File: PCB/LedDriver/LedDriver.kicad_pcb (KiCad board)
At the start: 2 copper layers, 125.7 x 125.7 mm, 189 parts, among them J101 LCD, J102 Conn_01x07_Female, J103 Conn_01x02_Male, J104 Conn_01x02_Male, J105 Conn_01x02_Male, J106 Conn_01x02_Male, J107 DC+5V, J108 Conn_01x08_Male, J109 Conn_01x08_Male, J110 Conn_01x08_Male, J111 Conn_01x02_Male, SW101 SW_Push, SW102 SW_Push, SW103 SW_Push, SW104 SW_Push, SW105 SW_Push, SW106 SW_Push, SW107 SW_Push, U101 MW-R-WX, U102 LM1117-3.3, U103 LM35-LP, U201 NJW4617DL3-TE1, U202 NJW4617DL3-TE1, U203 NJW4617DL3-TE1, U204 NJW4617DL3-TE1, U205 NJW4617DL3-TE1, U206 NJW4617DL3-TE1, U207 NJW4617DL3-TE1, U208 74HC595, U301 NJW4617DL3-TE1, U302 NJW4617DL3-TE1, U303 NJW4617DL3-TE1, U304 NJW4617DL3-TE1, U305 NJW4617DL3-TE1, U306 NJW4617DL3-TE1, U307 NJW4617DL3-TE1, U308 74HC595, U401 NJW4617DL3-TE1, U402 NJW4617DL3-TE1, U403 NJW4617DL3-TE1, U404 NJW4617DL3-TE1, U405 NJW4617DL3-TE1, U406 NJW4617DL3-TE1, U407 NJW4617DL3-TE1, U408 74HC595

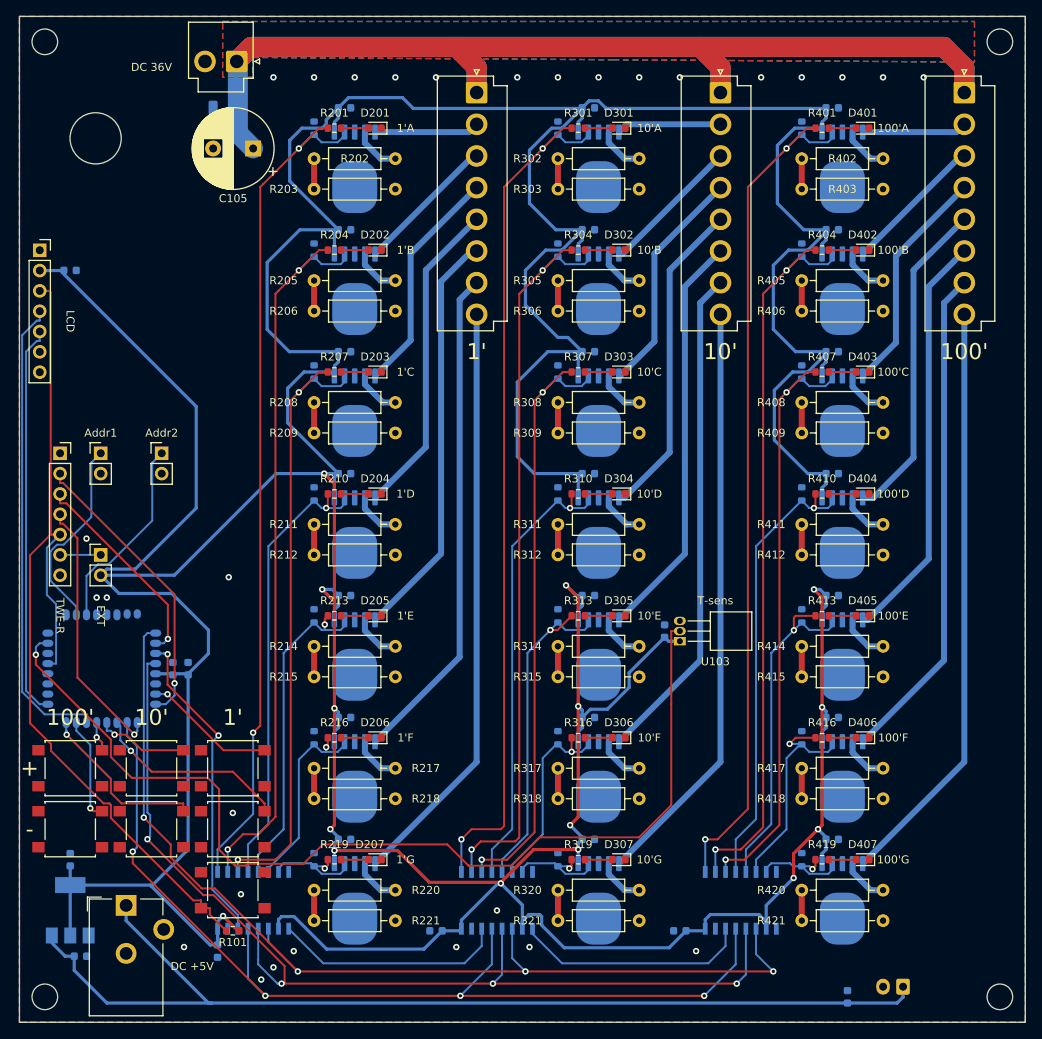
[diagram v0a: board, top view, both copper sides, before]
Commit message: パターン修正
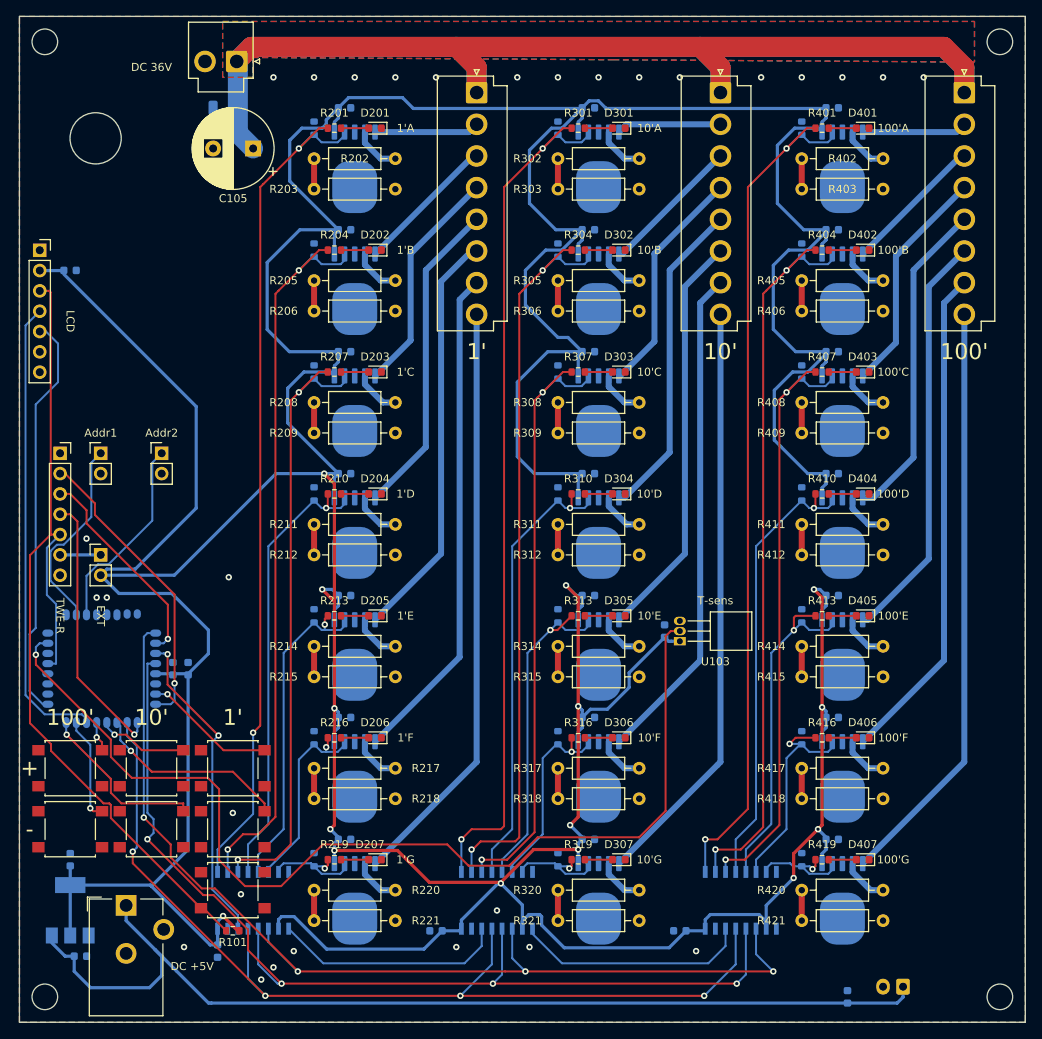
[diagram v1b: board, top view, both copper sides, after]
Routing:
- net /ADC1: track 127.6 -> 130.5 mm
- net Net-(C106-Pad1): track 129.9 -> 127.2 mm
- net /SDA: track 49.2 -> 50.8 mm
- net /SCL: track 58.9 -> 58.0 mm
- net /RESET: track 113.6 -> 113.0 mm
- net /RX: track 33.2 -> 33.8 mm
- net /TX: track 36.7 -> 37.2 mm
